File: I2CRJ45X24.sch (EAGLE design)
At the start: 123 parts, among them IC1 MCP23017SO, IC2 MCP23017SO, IC3 MCP23017SO, IC4 MCP23017SO, IC5 MCP23017SO, IC6 MCP23017SO, J1 RJ45-X8, J2 RJ45-X8, J3 RJ45-X8, J5 M06-PIN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

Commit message: Board and schematic labelling
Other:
- note added: "24 Channel I2C RJ45 Breakout"
- note added: "I2C Addresses: 0x20-0x25"
- note added: "RJ45 Pinout: 1: Data 1 2: Data 2 3: Data 3 4: VIN 5: VIN 6: Data 4 7: GND 8: GND"
- note added: "VIN: 12V VCC: 1.8-5.5V"
- note removed: "1: Data 1 2: Data 2 3: Data 3 4: VIN 5: VIN 6: Data 4 7: GND 8: GND"
- note removed: "I2C to 24 x RJ45 Breakout"
- moved on the sheet: D1, J4, J5, J6, J7, J8, LED1, R67, R68, R69, SJ2, SJ3

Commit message: Added fiducials and optimised GND pathways
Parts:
- added FID1, FID2, FID3: FIDUCIAL1X2.5, freetronics:FIDUCIAL1X2.5
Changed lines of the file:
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@@
 <part name="GND15" library="SuperHouse-SupplySymbols" library_urn="urn:adsk.eagle:library:11790503" deviceset="GND" device=""/>
 <part name="D1" library="SuperHouse-DiscreteSemi" library_urn="urn:adsk.eagle:library:11768461" deviceset="DIODE" device="SMA" package3d_urn="urn:adsk.eagle:package:7066222/3"/>
+<part name="FID1" library="freetronics" deviceset="FIDUCIAL" device="1X2.5"/>
+<part name="FID2" library="freetronics" deviceset="FIDUCIAL" device="1X2.5"/>
+<part name="FID3" library="freetronics" deviceset="FIDUCIAL" device="1X2.5"/>
 </parts>
 <sheets>
@@
 <attribute name="VALUE" x="101.6" y="78.9686" size="1.778" layer="96"/>
 </instance>
+<instance part="FID1" gate="G$1" x="137.16" y="7.62" smashed="yes"/>
+<instance part="FID2" gate="G$1" x="142.24" y="7.62" smashed="yes"/>
+<instance part="FID3" gate="G$1" x="132.08" y="7.62" smashed="yes"/>
 </instances>
 <busses>

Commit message: Final routing, plus ERC and DRC for v1.0 release
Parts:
- D1: value (none) -> SS56
- FID1, FID2, FID3: device freetronics:FIDUCIAL1X2.5 -> SuperHouse-Symbols:FIDUCIAL1X2.5
- J4: value (none) -> POWER
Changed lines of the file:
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@@
 <part name="C6" library="SuperHouse-DiscreteSemi" library_urn="urn:adsk.eagle:library:11768461" deviceset="CAP" device="0805" package3d_urn="urn:adsk.eagle:package:7066318/4" value="10uF"/>
 <part name="J5" library="SuperHouse-Connectors" library_urn="urn:adsk.eagle:library:11765989" deviceset="M06" device="-PIN" package3d_urn="urn:adsk.eagle:package:11790969/4"/>
-<part name="J6" library="SuperHouse-Connectors" library_urn="urn:adsk.eagle:library:11765989" deviceset="RJ45-X1" device="-METAL" package3d_urn="urn:adsk.eagle:package:12799247/3"/>
-<part name="J7" library="SuperHouse-Connectors" library_urn="urn:adsk.eagle:library:11765989" deviceset="RJ45-X1" device="-METAL" package3d_urn="urn:adsk.eagle:package:12799247/3"/>
+<part name="J6" library="SuperHouse-Connectors" library_urn="urn:adsk.eagle:library:11765989" deviceset="RJ45-X1" device="-METAL" package3d_urn="urn:adsk.eagle:package:12799247/5"/>
+<part name="J7" library="SuperHouse-Connectors" library_urn="urn:adsk.eagle:library:11765989" deviceset="RJ45-X1" device="-METAL" package3d_urn="urn:adsk.eagle:package:12799247/5"/>
 <part name="LED1" library="SuperHouse-LEDs" library_urn="urn:adsk.eagle:library:11790571" deviceset="LED" device="3MM" package3d_urn="urn:adsk.eagle:package:7066238/2" value="BLUE"/>
 <part name="GND10" library="SuperHouse-SupplySymbols" library_urn="urn:adsk.eagle:library:11790503" deviceset="GND" device=""/>
 <part name="R67" library="SuperHouse-DiscreteSemi" library_urn="urn:adsk.eagle:library:11768461" deviceset="RESISTOR" device="0603" package3d_urn="urn:adsk.eagle:package:11768543/2" value="1K5"/>
-<part name="J4" library="SuperHouse-Connectors" library_urn="urn:adsk.eagle:library:11765989" deviceset="M02" device="-SCREW-3.5MM" package3d_urn="urn:adsk.eagle:package:7066395/2"/>
+<part name="J4" library="SuperHouse-Connectors" library_urn="urn:adsk.eagle:library:11765989" deviceset="M02" device="-SCREW-3.5MM" package3d_urn="urn:adsk.eagle:package:7066395/2" value="POWER"/>
 <part name="J8" library="SuperHouse-Connectors" library_urn="urn:adsk.eagle:library:11765989" deviceset="POWER_JACK" device="-SLOTS" package3d_urn="urn:adsk.eagle:package:7066536/4"/>
 <part name="GND14" library="SuperHouse-SupplySymbols" library_urn="urn:adsk.eagle:library:11790503" deviceset="GND" device=""/>
 <part name="GND15" library="SuperHouse-SupplySymbols" library_urn="urn:adsk.eagle:library:11790503" deviceset="GND" device=""/>
-<part name="D1" library="SuperHouse-DiscreteSemi" library_urn="urn:adsk.eagle:library:11768461" deviceset="DIODE" device="SMA" package3d_urn="urn:adsk.eagle:package:7066222/3"/>
-<part name="FID1" library="freetronics" deviceset="FIDUCIAL" device="1X2.5"/>
-<part name="FID2" library="freetronics" deviceset="FIDUCIAL" device="1X2.5"/>
-<part name="FID3" library="freetronics" deviceset="FIDUCIAL" device="1X2.5"/>
+<part name="D1" library="SuperHouse-DiscreteSemi" library_urn="urn:adsk.eagle:library:11768461" deviceset="DIODE" device="SMA" package3d_urn="urn:adsk.eagle:package:7066222/3" value="SS56"/>
+<part name="FID1" library="SuperHouse-Symbols" library_urn="urn:adsk.eagle:library:13228893" deviceset="FIDUCIAL" device="1X2.5" package3d_urn="urn:adsk.eagle:package:13228898/1"/>
+<part name="FID2" library="SuperHouse-Symbols" library_urn="urn:adsk.eagle:library:13228893" deviceset="FIDUCIAL" device="1X2.5" package3d_urn="urn:adsk.eagle:package:13228898/1"/>
+<part name="FID3" library="SuperHouse-Symbols" library_urn="urn:adsk.eagle:library:13228893" deviceset="FIDUCIAL" device="1X2.5" package3d_urn="urn:adsk.eagle:package:13228898/1"/>
 </parts>
 <sheets>

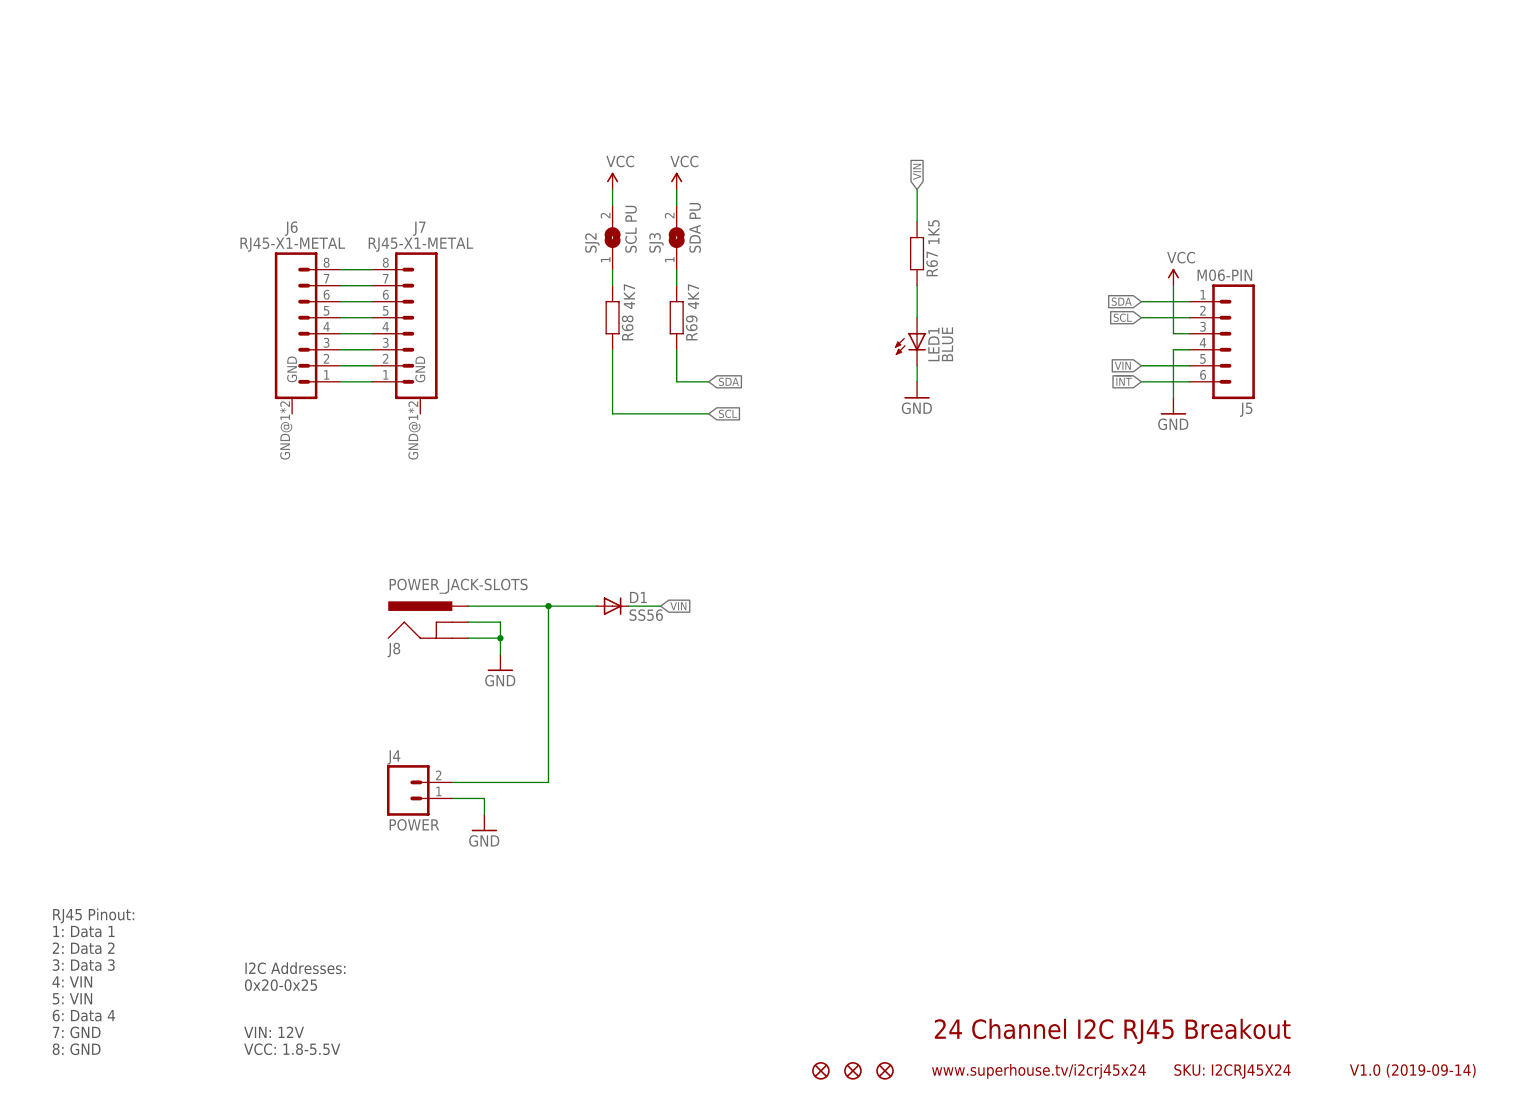
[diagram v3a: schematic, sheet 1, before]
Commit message: Converted to I2C-BREAKOUT header for v2.0 release
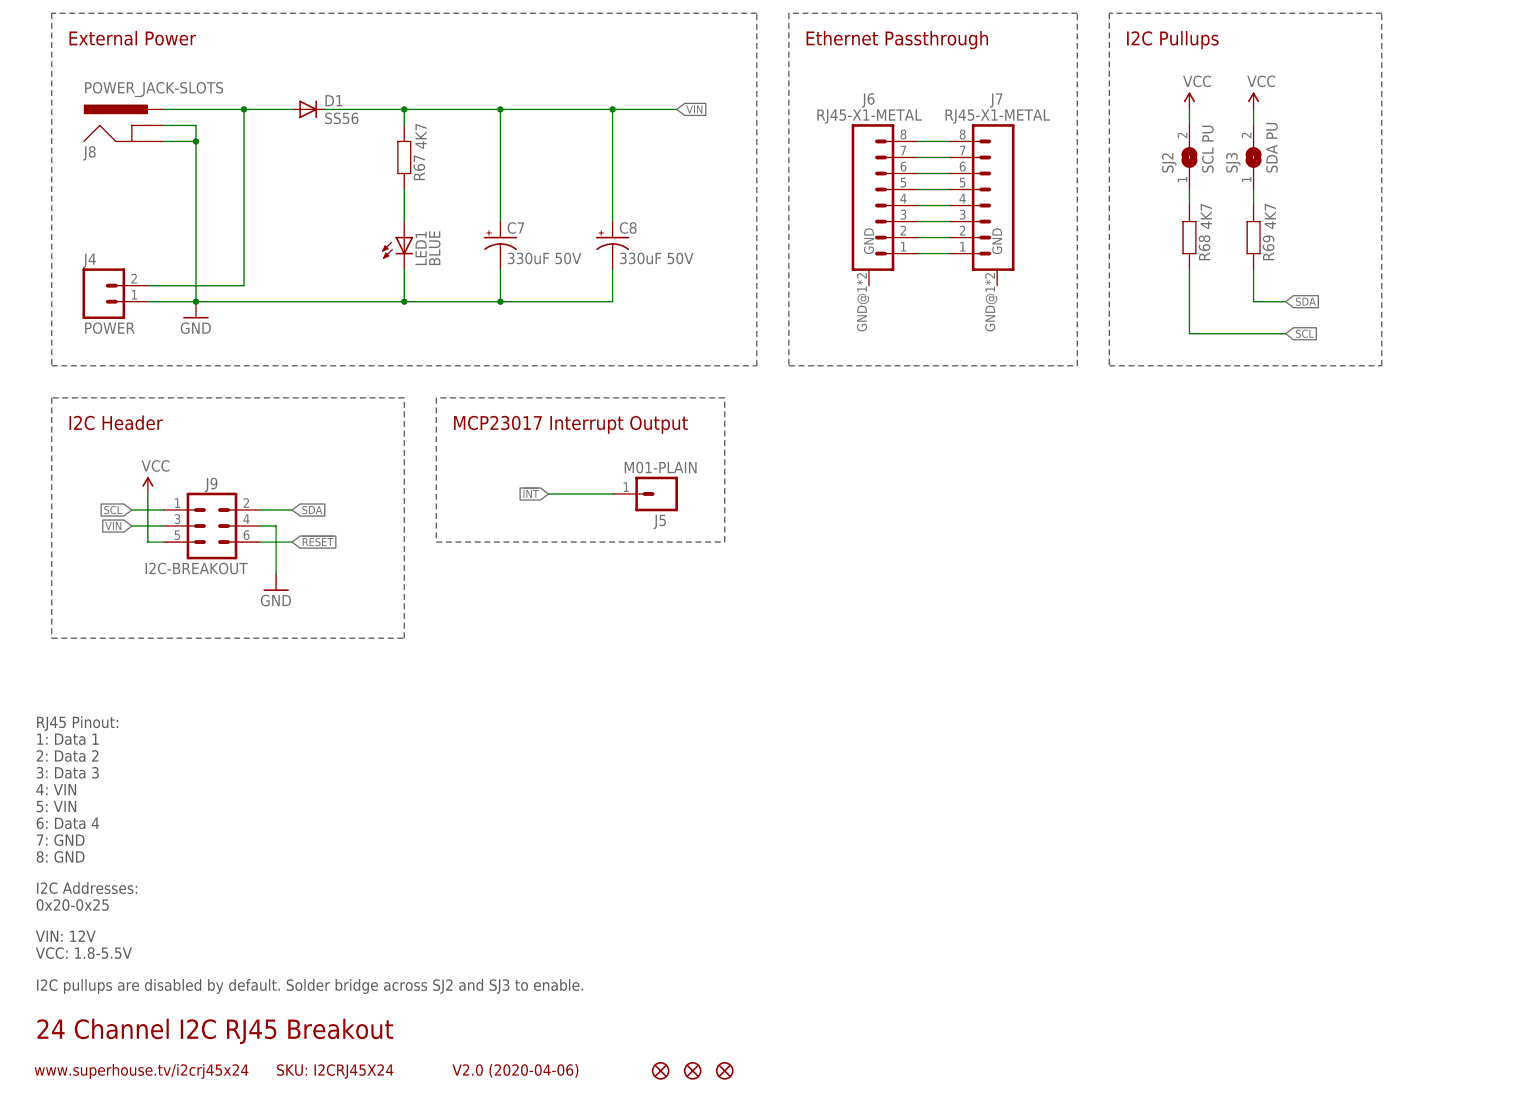
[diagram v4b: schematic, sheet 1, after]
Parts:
- added C7, C8: 330uF 50V, SuperHouse-DiscreteSemi:CAP_POLG
- added J9: I2C-BREAKOUT, SuperHouse-Connectors:M02X3-SHROUDED
- J5: value M06-PIN -> M01-PLAIN; device SuperHouse-Connectors:M06-PIN -> SuperHouse-Connectors:M01-PLAIN
- R67: value 1K5 -> 4K7
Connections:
- new net !RESET: IC1.!RESET, IC2.!RESET, IC3.!RESET, IC4.!RESET, IC5.!RESET, IC6.!RESET, J9.6
- net !INT: now also J5.1; no longer J5.6
- net GND: now also C7.-, C8.-, J9.4; no longer J5.4
- net SCL: now also J9.1; no longer J5.2
- net SDA: now also J9.2; no longer J5.1
- net VCC: now also J9.5; no longer IC1.!RESET, IC2.!RESET, IC3.!RESET, IC4.!RESET, IC5.!RESET, IC6.!RESET, J5.3
- net VIN: now also C7.+, C8.+, J9.3; no longer J5.5
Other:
- note added: "Ethernet Passthrough"
- note added: "External Power"
- note added: "I2C Header"
- note added: "I2C Pullups"
- note added: "I2C pullups are disabled by default. Solder bridge across SJ2 and SJ3 to enable."
- note added: "MCP23017 Interrupt Output"
- note added: "V2.0 (2020-04-06)"
- note removed: "V1.0 (2019-09-14)"
- moved on the sheet: D1, J4, J6, J7, J8, LED1, R67, R68, R69, SJ2, SJ3

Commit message: Moved holes back from edge for v2.1 release
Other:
- note added: "V2.1 (2020-04-13)"
- note removed: "V2.0 (2020-04-06)"
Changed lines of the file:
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@@
 <frame x1="0" y1="0" x2="248.92" y2="185.42" columns="8" rows="5" layer="94"/>
 <text x="7.62" y="12.7" size="3.048" layer="94">24 Channel I2C RJ45 Breakout</text>
-<text x="73.66" y="6.858" size="1.778" layer="94">V2.0 (2020-04-06)</text>
+<text x="73.66" y="6.858" size="1.778" layer="94">V2.1 (2020-04-13)</text>
 <text x="7.366" y="6.858" size="1.778" layer="94">www.superhouse.tv/i2crj45x24</text>
 <text x="45.72" y="6.858" size="1.778" layer="94">SKU: I2CRJ45X24</text>

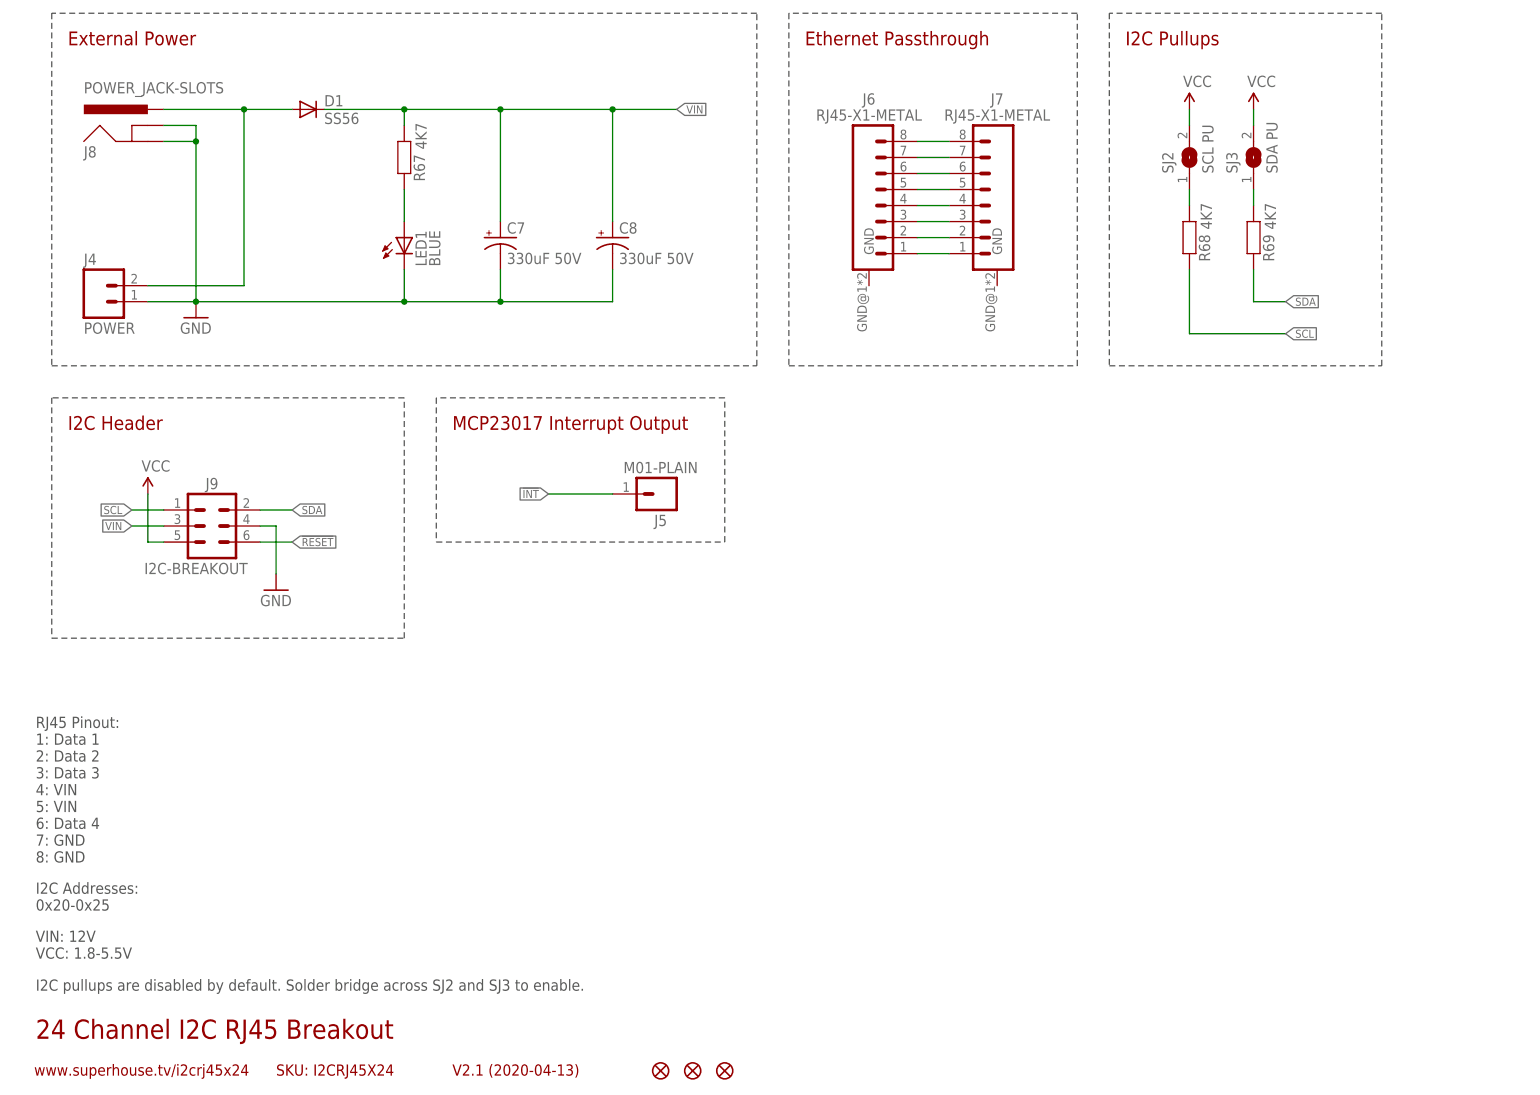
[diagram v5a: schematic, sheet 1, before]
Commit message: Removed Ethernet passthrough and shortened board.
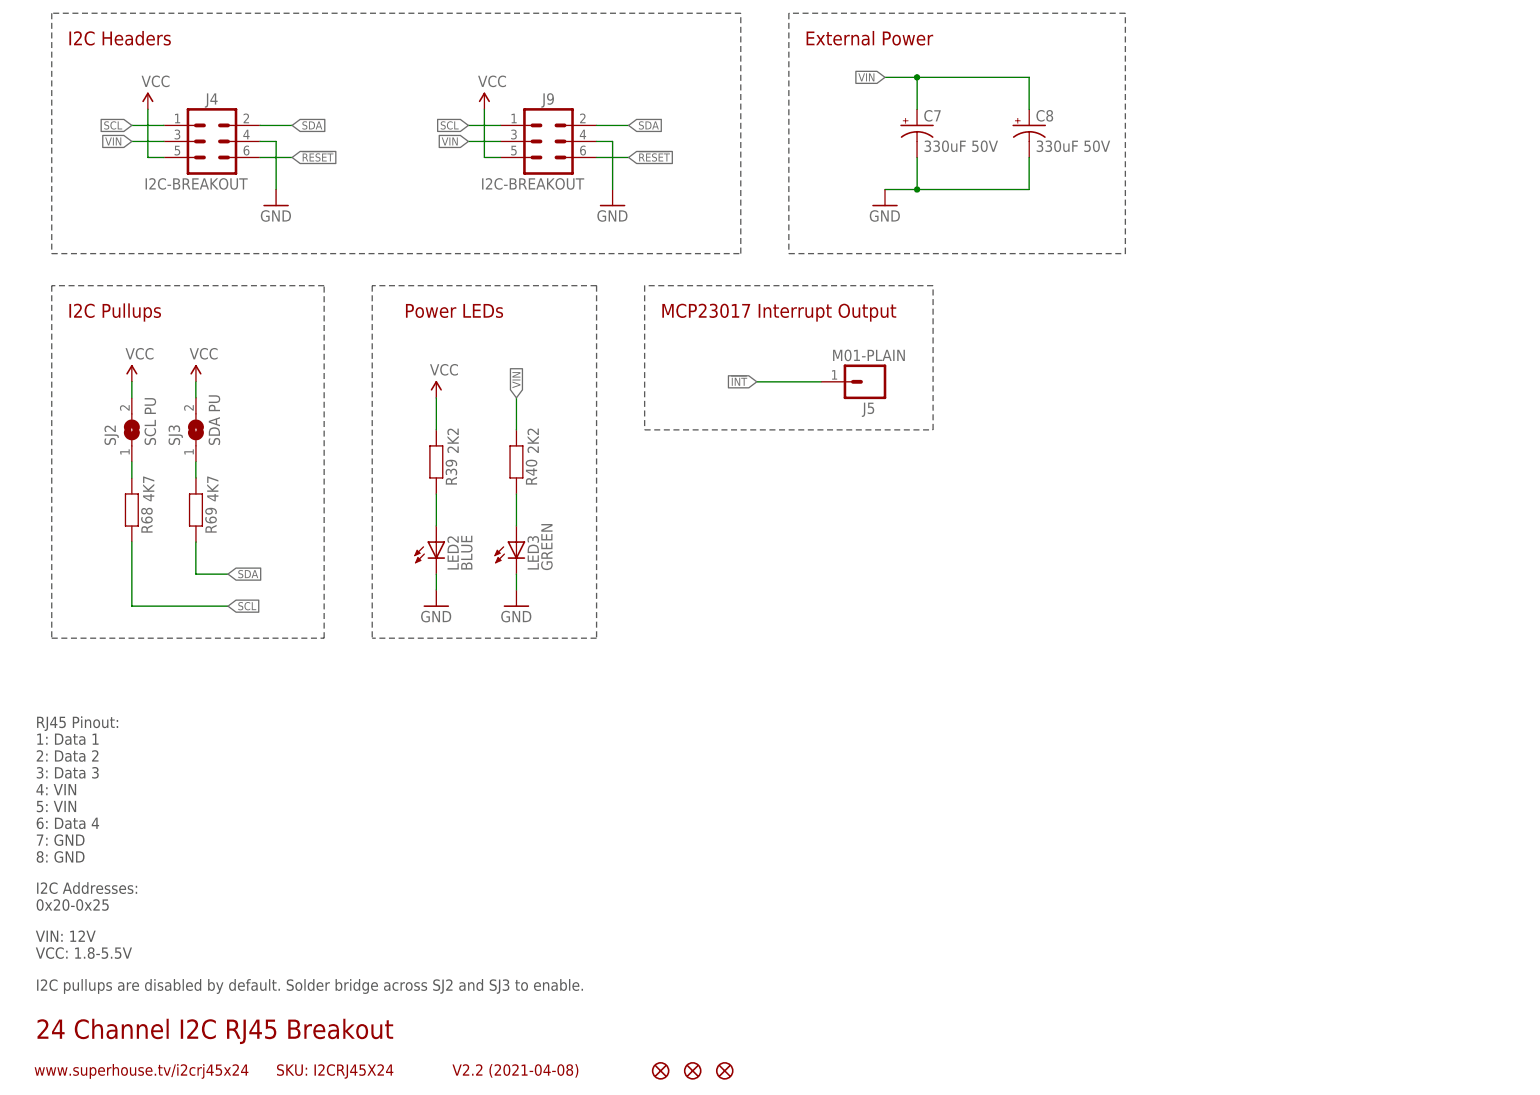
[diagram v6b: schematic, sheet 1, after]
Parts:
- removed D1: SS56, SuperHouse-DiscreteSemi:DIODESMA
- removed J6, J7: RJ45-X1-METAL, SuperHouse-Connectors:RJ45-X1-METAL
- removed J8: POWER_JACK-SLOTS, SuperHouse-Connectors:POWER_JACK-SLOTS
- removed LED1: BLUE, SuperHouse-LEDs:LED3MM
- removed R67: 4K7, SuperHouse-DiscreteSemi:RESISTOR0603
- added LED2: BLUE, SuperHouse-LEDs:LED0603
- added LED3: GREEN, SuperHouse-LEDs:LED0603
- added R39, R40: 2K2, SuperHouse-DiscreteSemi:RESISTOR0603
- J4: value POWER -> I2C-BREAKOUT; device SuperHouse-Connectors:M02-SCREW-3.5MM -> SuperHouse-Connectors:M02X3-SHROUDED
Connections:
- removed net N$10: J6.6, J7.6
- removed net N$11: J6.7, J7.7
- removed net N$12: J6.8, J7.8
- removed net N$13: LED1.A, R67.1
- removed net N$18: D1.A, J4.2, J8.PWR
- removed net N$3: J6.1, J7.1
- removed net N$4: J6.2, J7.2
- removed net N$5: J6.3, J7.3
- removed net N$6: J6.4, J7.4
- removed net N$9: J6.5, J7.5
- new net N$7: LED2.A, R39.1
- new net N$8: LED3.A, R40.1
- net !RESET: now also J4.6
- net GND: now also J4.4, LED2.C, LED3.C; no longer J4.1, J8.GND, J8.GNDBREAK, LED1.C
- net SCL: now also J4.1
- net SDA: now also J4.2
- net VCC: now also J4.5, R39.2
- net VIN: now also J4.3, R40.2; no longer D1.C, R67.2
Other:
- note added: "I2C Headers"
- note added: "Power LEDs"
- note added: "V2.2 (2021-04-08)"
- note removed: "Ethernet Passthrough"
- note removed: "I2C Header"
- note removed: "V2.1 (2020-04-13)"
- moved on the sheet: C7, C8, J5, J9, R68, R69, SJ2, SJ3
